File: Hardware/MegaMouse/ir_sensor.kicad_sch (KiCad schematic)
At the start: 1 part

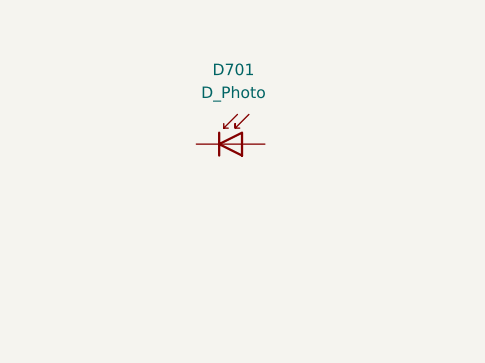
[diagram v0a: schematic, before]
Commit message: Add inital photodiodes
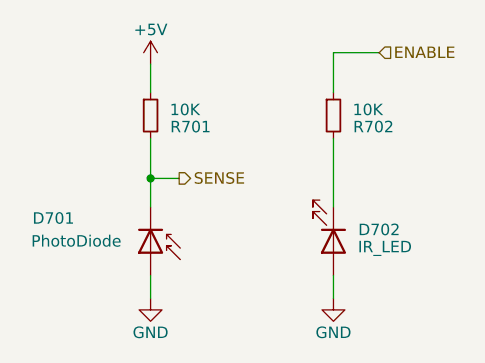
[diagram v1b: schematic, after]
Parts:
- added D702: IR_LED, LED_THT:LED_D5.0mm_Horizontal_O1.27mm_Z3.0mm_Clear, symbol Device:LED
- added R701, R702: 10K, Resistor_SMD:R_0805_2012Metric, symbol Device:R_Small
- D701: value D_Photo -> PhotoDiode
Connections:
- net SENSE: now reaches D701.1 (K)
- net SENSE: now also R701.2
- net GND: now reaches D701.2 (A)
- net GND: now also D702.2 (A)
- new net: D702.1 (K), R702.2
- new net +5V: R701.1
- new net ENABLE: R702.1
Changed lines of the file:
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@@
 (kicad_sch (version 20211123) (generator eeschema)
   (paper "A4")
-  (symbol (lib_id "Device:D_Photo") (at 136.525 95.885 0) (unit 1)
-    (in_bom yes) (on_board yes) (fields_autoplaced)
-    (property "Reference" "D701" (id 0) (at 135.5725 87.63 0))
-    (property "Value" "D_Photo" (id 1) (at 135.5725 90.17 0))
-    (property "Footprint" "LED_THT:LED_D5.0mm_Horizontal_O1.27mm_Z3.0mm_IRBlack" (id 2) (at 135.255 95.885 0)
+  (junction (at 126.365 99.695) (diameter 0) (color 0 0 0 0)
+  )
+  (wire (pts (xy 151.765 85.725) (xy 146.685 85.725))
+    (stroke (width 0) (type default) (color 0 0 0 0))
+  )
+  (wire (pts (xy 126.365 110.49) (xy 126.365 113.03))
+    (stroke (width 0) (type default) (color 0 0 0 0))
+  )
+  (wire (pts (xy 126.365 95.25) (xy 126.365 99.695))
+    (stroke (width 0) (type default) (color 0 0 0 0))
+  )
+  (wire (pts (xy 126.365 99.695) (xy 126.365 102.87))
+    (stroke (width 0) (type default) (color 0 0 0 0))
+  )
+  (wire (pts (xy 146.685 110.49) (xy 146.685 113.03))
+    (stroke (width 0) (type default) (color 0 0 0 0))
+  )
+  (wire (pts (xy 146.685 85.725) (xy 146.685 90.17))
+    (stroke (width 0) (type default) (color 0 0 0 0))
+  )
+  (wire (pts (xy 126.365 99.695) (xy 129.54 99.695))
+    (stroke (width 0) (type default) (color 0 0 0 0))
+  )
+  (wire (pts (xy 126.365 86.995) (xy 126.365 90.17))
+    (stroke (width 0) (type default) (color 0 0 0 0))
+  )
+  (wire (pts (xy 146.685 95.25) (xy 146.685 102.87))
+    (stroke (width 0) (type default) (color 0 0 0 0))
+  )
+  (hierarchical_label "SENSE" (shape output) (at 129.54 99.695 0)
+    (effects (font (size 1.27 1.27)) (justify left))
+  )
+  (hierarchical_label "ENABLE" (shape input) (at 151.765 85.725 0)
+    (effects (font (size 1.27 1.27)) (justify left))
+  )
+  (symbol (lib_id "power:GND") (at 126.365 113.03 0) (unit 1)
+    (in_bom yes) (on_board yes)
+    (property "Reference" "#PWR0702" (id 0) (at 126.365 119.38 0)
       (effects (font (size 1.27 1.27)) hide)
     )
-    (property "Datasheet" "~" (id 3) (at 135.255 95.885 0)
+    (property "Value" "GND" (id 1) (at 126.365 116.84 0))
+    (property "Footprint" "" (id 2) (at 126.365 113.03 0)
       (effects (font (size 1.27 1.27)) hide)
     )
+    (property "Datasheet" "" (id 3) (at 126.365 113.03 0)
+      (effects (font (size 1.27 1.27)) hide)
+    )
+    (pin "1")
+  )
+  (symbol (lib_id "Device:LED") (at 146.685 106.68 270) (unit 1)
+    (in_bom yes) (on_board yes)
+    (property "Reference" "D702" (id 0) (at 151.765 105.41 90))
+    (property "Value" "IR_LED" (id 1) (at 152.4 107.315 90))
+    (property "Footprint" "LED_THT:LED_D5.0mm_Horizontal_O1.27mm_Z3.0mm_Clear" (id 2) (at 146.685 106.68 0)
+      (effects (font (size 1.27 1.27)) hide)
+    )
+    (property "Datasheet" "~" (id 3) (at 146.685 106.68 0)
+      (effects (font (size 1.27 1.27)) hide)
+    )
+    (pin "1")
+    (pin "2")
+  )
+  (symbol (lib_id "Device:R_Small") (at 146.685 92.71 0) (unit 1)
+    (in_bom yes) (on_board yes)
+    (property "Reference" "R702" (id 0) (at 151.13 93.98 0))
+    (property "Value" "10K" (id 1) (at 150.495 92.075 0))
+    (property "Footprint" "Resistor_SMD:R_0805_2012Metric" (id 2) (at 146.685 92.71 0)
+      (effects (font (size 1.27 1.27)) hide)
+    )
+    (property "Datasheet" "~" (id 3) (at 146.685 92.71 0)
+      (effects (font (size 1.27 1.27)) hide)
+    )
+    (pin "1")
+    (pin "2")
+  )
+  (symbol (lib_id "Device:D_Photo") (at 126.365 107.95 270) (unit 1)
+    (in_bom yes) (on_board yes)
+    (property "Reference" "D701" (id 0) (at 115.57 104.14 90))
+    (property "Value" "PhotoDiode" (id 1) (at 118.11 106.68 90))
+    (property "Footprint" "LED_THT:LED_D5.0mm_Horizontal_O1.27mm_Z3.0mm_IRBlack" (id 2) (at 126.365 106.68 0)
+      (effects (font (size 1.27 1.27)) hide)
+    )
+    (property "Datasheet" "~" (id 3) (at 126.365 106.68 0)
+      (effects (font (size 1.27 1.27)) hide)
+    )
+    (pin "1")
+    (pin "2")
+  )
+  (symbol (lib_id "power:GND") (at 146.685 113.03 0) (unit 1)
+    (in_bom yes) (on_board yes)
+    (property "Reference" "#PWR0703" (id 0) (at 146.685 119.38 0)
+      (effects (font (size 1.27 1.27)) hide)
+    )
+    (property "Value" "GND" (id 1) (at 146.685 116.84 0))
+    (property "Footprint" "" (id 2) (at 146.685 113.03 0)
+      (effects (font (size 1.27 1.27)) hide)
+    )
+    (property "Datasheet" "" (id 3) (at 146.685 113.03 0)
+      (effects (font (size 1.27 1.27)) hide)
+    )
+    (pin "1")
+  )
+  (symbol (lib_id "power:+5V") (at 126.365 86.995 0) (unit 1)
+    (in_bom yes) (on_board yes)
+    (property "Reference" "#PWR0701" (id 0) (at 126.365 90.805 0)
+      (effects (font (size 1.27 1.27)) hide)
+    )
+    (property "Value" "+5V" (id 1) (at 126.365 83.185 0))
+    (property "Footprint" "" (id 2) (at 126.365 86.995 0)
+      (effects (font (size 1.27 1.27)) hide)
+    )
+    (property "Datasheet" "" (id 3) (at 126.365 86.995 0)
+      (effects (font (size 1.27 1.27)) hide)
+    )
+    (pin "1")
+  )
+  (symbol (lib_id "Device:R_Small") (at 126.365 92.71 0) (unit 1)
+    (in_bom yes) (on_board yes)
+    (property "Reference" "R701" (id 0) (at 130.81 93.98 0))
+    (property "Value" "10K" (id 1) (at 130.175 92.075 0))
+    (property "Footprint" "Resistor_SMD:R_0805_2012Metric" (id 2) (at 126.365 92.71 0)
+      (effects (font (size 1.27 1.27)) hide)
+    )
+    (property "Datasheet" "~" (id 3) (at 126.365 92.71 0)
+      (effects (font (size 1.27 1.27)) hide)
+    )

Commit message: Add in some more, random junk
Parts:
- added RV701: 10K, Potentiometer_SMD:Potentiometer_Bourns_TC33X_Vertical, symbol Device:R_Potentiometer
- R701: value 10K -> DNP
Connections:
- net +5V: now also RV701.1
- net GND: now also D702.1 (K); no longer D702.2 (A)
- net SENSE: now also RV701.2
- net at R702.2: now also D702.2 (A); no longer D702.1 (K)
- no-connect marks 0 -> 1
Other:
- moved on the sheet: D702
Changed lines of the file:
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@@
 (kicad_sch (version 20211123) (generator eeschema)
   (paper "A4")
+  (junction (at 126.365 97.155) (diameter 0) (color 0 0 0 0)
+  )
   (junction (at 126.365 99.695) (diameter 0) (color 0 0 0 0)
   )
+  (junction (at 126.365 88.9) (diameter 0) (color 0 0 0 0)
+  )
+  (no_connect (at 115.57 100.965))
   (wire (pts (xy 151.765 85.725) (xy 146.685 85.725))
+    (stroke (width 0) (type default) (color 0 0 0 0))
+  )
+  (wire (pts (xy 126.365 88.9) (xy 126.365 90.17))
     (stroke (width 0) (type default) (color 0 0 0 0))
   )
@@
     (stroke (width 0) (type default) (color 0 0 0 0))
   )
-  (wire (pts (xy 126.365 95.25) (xy 126.365 99.695))
+  (wire (pts (xy 126.365 95.25) (xy 126.365 97.155))
     (stroke (width 0) (type default) (color 0 0 0 0))
   )
   (wire (pts (xy 126.365 99.695) (xy 126.365 102.87))
+    (stroke (width 0) (type default) (color 0 0 0 0))
+  )
+  (wire (pts (xy 115.57 88.9) (xy 115.57 93.345))
     (stroke (width 0) (type default) (color 0 0 0 0))
   )
@@
     (stroke (width 0) (type default) (color 0 0 0 0))
   )
+  (wire (pts (xy 126.365 88.9) (xy 115.57 88.9))
+    (stroke (width 0) (type default) (color 0 0 0 0))
+  )
+  (wire (pts (xy 126.365 97.155) (xy 126.365 99.695))
+    (stroke (width 0) (type default) (color 0 0 0 0))
+  )
+  (wire (pts (xy 119.38 97.155) (xy 126.365 97.155))
+    (stroke (width 0) (type default) (color 0 0 0 0))
+  )
   (wire (pts (xy 126.365 99.695) (xy 129.54 99.695))
     (stroke (width 0) (type default) (color 0 0 0 0))
   )
-  (wire (pts (xy 126.365 86.995) (xy 126.365 90.17))
+  (wire (pts (xy 126.365 86.995) (xy 126.365 88.9))
     (stroke (width 0) (type default) (color 0 0 0 0))
   )
@@
     (pin "1")
   )
-  (symbol (lib_id "Device:LED") (at 146.685 106.68 270) (unit 1)
+  (symbol (lib_id "Device:R_Potentiometer") (at 115.57 97.155 0) (unit 1)
+    (in_bom yes) (on_board yes) (fields_autoplaced)
+    (property "Reference" "RV701" (id 0) (at 113.03 95.8849 0)
+      (effects (font (size 1.27 1.27)) (justify right))
+    )
+    (property "Value" "10K" (id 1) (at 113.03 98.4249 0)
+      (effects (font (size 1.27 1.27)) (justify right))
+    )
+    (property "Footprint" "Potentiometer_SMD:Potentiometer_Bourns_TC33X_Vertical" (id 2) (at 115.57 97.155 0)
+      (effects (font (size 1.27 1.27)) hide)
+    )
+    (property "Datasheet" "~" (id 3) (at 115.57 97.155 0)
+      (effects (font (size 1.27 1.27)) hide)
+    )
+    (property "LCSC" "https://www.lcsc.com/product-detail/Variable-Resistors-Potentiometers_HDK-Hokuriku-Elec-Industry-VG039NSNXTB103_C515300.html" (id 4) (at 115.57 97.155 0)
+      (effects (font (size 1.27 1.27)) hide)
+    )
+    (pin "1")
+    (pin "2")
+    (pin "3")
+  )
+  (symbol (lib_id "Device:LED") (at 146.685 106.68 90) (unit 1)
     (in_bom yes) (on_board yes)
-    (property "Reference" "D702" (id 0) (at 151.765 105.41 90))
-    (property "Value" "IR_LED" (id 1) (at 152.4 107.315 90))
+    (property "Reference" "D702" (id 0) (at 153.035 107.95 90))
+    (property "Value" "IR_LED" (id 1) (at 152.4 106.045 90))
     (property "Footprint" "LED_THT:LED_D5.0mm_Horizontal_O1.27mm_Z3.0mm_Clear" (id 2) (at 146.685 106.68 0)
       (effects (font (size 1.27 1.27)) hide)
@@
   (symbol (lib_id "Device:D_Photo") (at 126.365 107.95 270) (unit 1)
     (in_bom yes) (on_board yes)
-    (property "Reference" "D701" (id 0) (at 115.57 104.14 90))
-    (property "Value" "PhotoDiode" (id 1) (at 118.11 106.68 90))
+    (property "Reference" "D701" (id 0) (at 115.57 106.045 90))
+    (property "Value" "PhotoDiode" (id 1) (at 118.11 108.585 90))
     (property "Footprint" "LED_THT:LED_D5.0mm_Horizontal_O1.27mm_Z3.0mm_IRBlack" (id 2) (at 126.365 106.68 0)
       (effects (font (size 1.27 1.27)) hide)
@@
     (in_bom yes) (on_board yes)
     (property "Reference" "R701" (id 0) (at 130.81 93.98 0))
-    (property "Value" "10K" (id 1) (at 130.175 92.075 0))
+    (property "Value" "DNP" (id 1) (at 130.175 92.075 0))
     (property "Footprint" "Resistor_SMD:R_0805_2012Metric" (id 2) (at 126.365 92.71 0)
       (effects (font (size 1.27 1.27)) hide)

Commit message: Remove LCSC to fix builds
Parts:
- RV701: LCSC https://www.lcsc.com/product-detail/Variable-Resistors-Pote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 -> (none)
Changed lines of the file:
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@@
-      (effects (font (size 1.27 1.27)) hide)
-    )
-    (property "LCSC" "https://www.lcsc.com/product-detail/Variable-Resistors-Potentiometers_HDK-Hokuriku-Elec-Industry-VG039NSNXTB103_C515300.html" (id 4) (at 115.57 97.155 0)
       (effects (font (size 1.27 1.27)) hide)
     )

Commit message: Carlstrom Review (#2)
Thank you to Professor Carlstrom for reviewing!
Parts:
- added H801: Screw Adjust Hole, symbol Mechanical:MountingHole
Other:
- note added: "In place of the potentiometer. You can install this resistor if an appropriate constant value is found."
- note added: "The IR LED emits light whenever ENABLE is high. It consumes a similar level of current as a red LED."
- note added: "This direction should be correct, as the photodiode accepts more light, it conducts backwards like this."
- company: (none) -> Kitsune Scientific
- title: (none) -> MegaMouse
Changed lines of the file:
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@@
 (kicad_sch (version 20211123) (generator eeschema)
   (paper "A4")
+  (title_block
+    (title "MegaMouse")
+    (date "${ISSUE}")
+    (rev "${REVISION}")
+    (company "Kitsune Scientific")
+    (comment 4 "Release: ${FULL_REVISION}")
+  )
   (junction (at 126.365 97.155) (diameter 0) (color 0 0 0 0)
   )
@@
     (stroke (width 0) (type default) (color 0 0 0 0))
   )
+  (text "This direction should be correct,\nas the photodiode accepts more light,\nit conducts backwards like this."
+    (at 86.36 117.475 0)
+    (effects (font (size 1.27 1.27)) (justify left bottom))
+  )
+  (text "The IR LED emits light whenever\nENABLE is high.\nIt consumes a similar level of current\nas a red LED."
+    (at 150.495 119.38 0)
+    (effects (font (size 1.27 1.27)) (justify left bottom))
+  )
+  (text "In place of the potentiometer.\nYou can install this resistor\nif an appropriate constant value\nis found."
+    (at 89.535 88.9 0)
+    (effects (font (size 1.27 1.27)) (justify left bottom))
+  )
   (hierarchical_label "SENSE" (shape output) (at 129.54 99.695 0)
     (effects (font (size 1.27 1.27)) (justify left))
@@
     (pin "1")
   )
+  (symbol (lib_id "Mechanical:MountingHole") (at 15.24 194.31 0) (unit 1)
+    (in_bom yes) (on_board yes) (fields_autoplaced)
+    (property "Reference" "H801" (id 0) (at 18.415 193.0399 0)
+      (effects (font (size 1.27 1.27)) (justify left))
+    )
+    (property "Value" "Screw Adjust Hole" (id 1) (at 18.415 195.5799 0)
+      (effects (font (size 1.27 1.27)) (justify left))
+    )
+    (property "Footprint" "" (id 2) (at 15.24 194.31 0)
+      (effects (font (size 1.27 1.27)) hide)
+    )
+    (property "Datasheet" "~" (id 3) (at 15.24 194.31 0)
+      (effects (font (size 1.27 1.27)) hide)
+    )
+  )
   (symbol (lib_id "Device:R_Potentiometer") (at 115.57 97.155 0) (unit 1)

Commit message: Verification 1 (#3)
And thats all we have time for folks.
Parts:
- added R701: 330R, Resistor_SMD:R_0805_2012Metric, symbol Device:R_Small
- H701: renamed from H801; footprint (none) -> MountingHole:MountingHole_3mm
- renumbered R701 to R702, R702 to R703
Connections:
- net +5V: now also R701.1; no longer RV701.1
- new net: R701.2, RV701.1
